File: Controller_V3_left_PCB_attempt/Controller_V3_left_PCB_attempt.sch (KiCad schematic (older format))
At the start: 24 parts, among them IC1 ATTINY24-SS, U1 MAX1811, U2 MAX1595, X2 8MHz

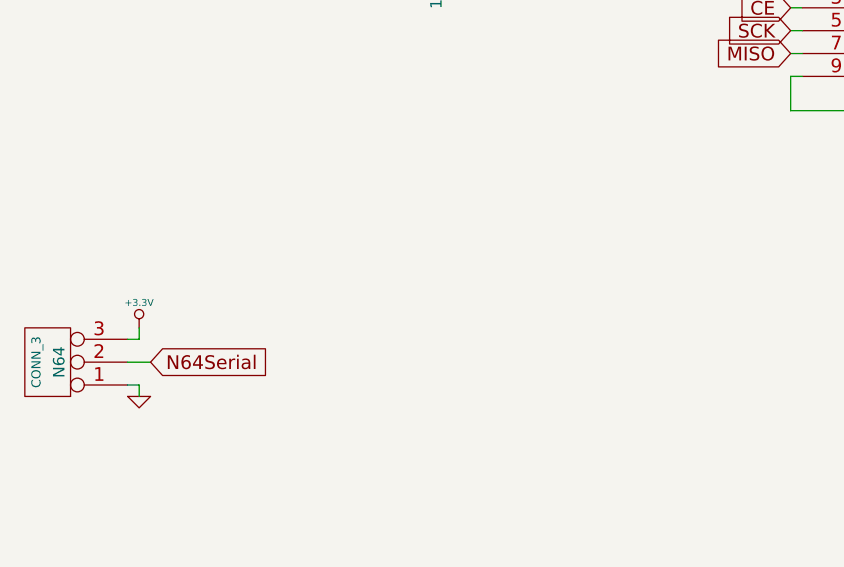
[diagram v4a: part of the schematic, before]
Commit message: added current consumption note on N64-controller.. is this a deal breaker
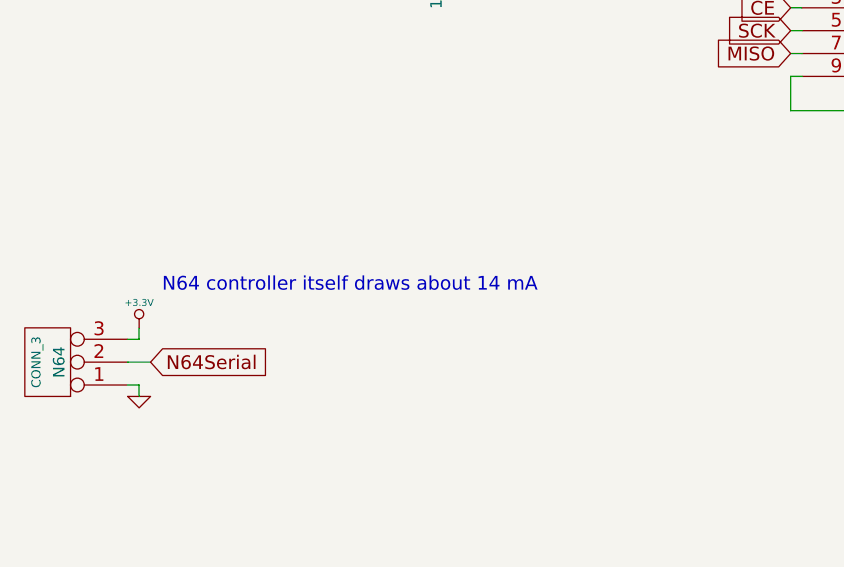
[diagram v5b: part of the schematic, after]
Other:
- note added: "N64 controller itself draws about 14 mA"
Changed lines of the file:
@@
-EESchema Schematic File Version 2  date 10-10-2012 09:57:18
+EESchema Schematic File Version 2  date 11-10-2012 13:37:10
 LIBS:power
 LIBS:device
@@
 Sheet 1 1
 Title ""
-Date "10 oct 2012"
+Date "11 oct 2012"
 Rev ""
 Comp ""
@@
 Comment4 ""
 $EndDescr
+Text Notes 4450 3800 0    60   ~ 0
+N64 controller itself draws about 14 mA
 Wire Wire Line
 	2150 6250 2150 6500
